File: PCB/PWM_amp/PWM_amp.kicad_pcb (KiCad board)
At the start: 4 copper layers, 84 x 84 mm, 59 parts, among them J1 Conn_01x07_Pin, J10 XT30UPB-M, J3 Conn_01x02_Pin, J4 Conn_01x02_Pin, J49 XT60PW-M, J5 XT30UPB-M, J6 Conn_01x07_Pin, Q1 FDD8447L, Q2 FDD8447L, U1 VNH5019A-E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

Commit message: 2.0.2 silkscreen edits
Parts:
- moved G*** 40.2 mm to (211.7, 121.2)
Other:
- board text added: "25/Mar 2026 Iter. 2.0.2"
- board text added: "Lin Lab"
- board text added: "Wei Yue Yucheng Yang PCB by Kevin Ying Nikita Lukhanin⁩ Divij Muthu Tofic Esses"
- board text removed: "24/Mar 2026 Iter. 2.0.1"
- board text removed: "Lin Lab Wei Yue Yucheng Yang PCB by Kevin Ying ⁨Nikita Lukhanin⁩ Divij Muthu Tofic Esses"

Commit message: generated prod files
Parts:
- moved VM 0.97 mm to (238.6, 88.7)
- moved C6 0.67 mm to (233.5, 87.6)
- moved J3 0.27 mm to (203.8, 99.9)
- moved J4 0.27 mm to (203.8, 134.0)
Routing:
- net PGND1: track 3.09 -> 8.01 mm, vias 208 -> 207
- net VM1: track 55.0 -> 57.2 mm, vias 67 -> 68
- net Net-(J4-Pin_1): track 46.1 -> 47.7 mm
- net Net-(J4-Pin_2): track 34.0 -> 35.6 mm
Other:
- board text added: "<A"
- board text added: "<B"

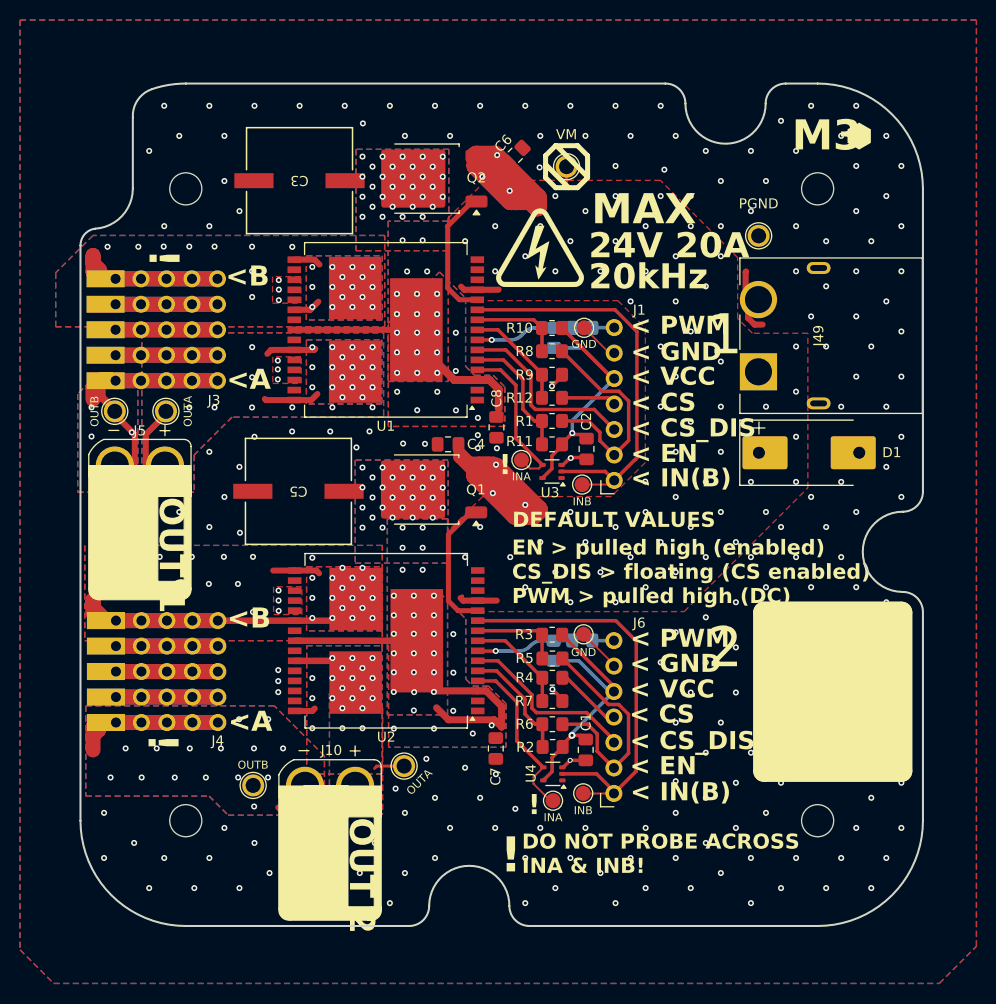
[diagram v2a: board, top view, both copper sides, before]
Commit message: ver 2.0.3: edge cut edits
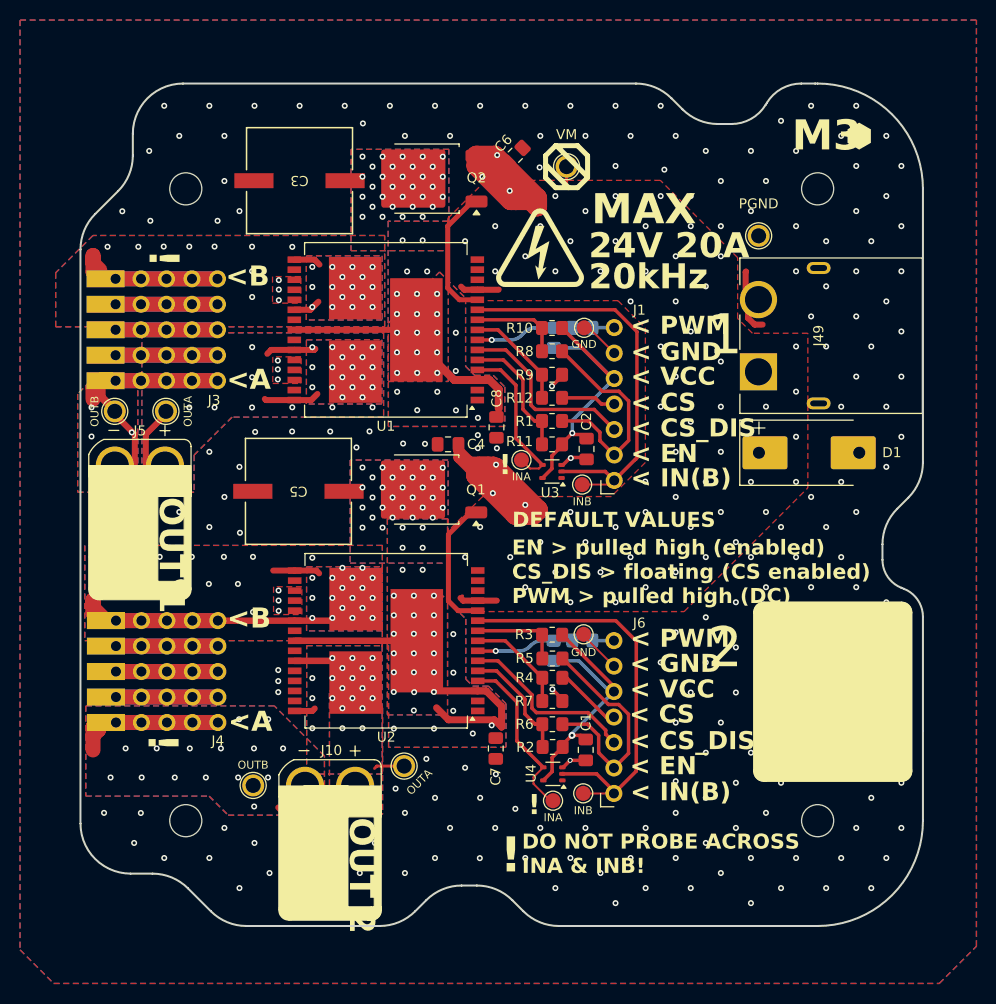
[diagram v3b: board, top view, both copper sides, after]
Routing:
- net GND1: track 18.2 -> 17.3 mm
- net PGND1: vias 207 -> 204
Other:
- outline, holes or cut-outs redrawn
- board text added: "25/Mar 2026 Iter. 2.0.3"
- board text removed: "25/Mar 2026 Iter. 2.0.2"

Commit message: 2.0.4 final touches
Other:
- board text added: "27/Mar 2026 Iter. 2.0.4"
- board text added: "CAUTION"
- board text removed: "25/Mar 2026 Iter. 2.0.3"

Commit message: 2.0.5
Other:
- board text added: "30/Mar 2026 Iter. 2.0.5"
- board text removed: "27/Mar 2026 Iter. 2.0.4"
